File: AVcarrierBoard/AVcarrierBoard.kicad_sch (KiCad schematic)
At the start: 16 parts, among them J1 Mech_Switch, J2 Mech_Switch, J3 MainRecov, J4 DrogRecov, J5 Staging, J6 Mech_Switch, U2 WiFi Switch, U3 EggtimerQuantum, U4 EggfinderMini/FeatherGPS, U5 Blue_Raven

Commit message: final edits made, order placed
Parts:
- BT1: symbol Device:Battery -> COTS_boards:Battery
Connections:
- net GND: now also BT1.3 (-); no longer BT1.2 (-)
- new net: BT1.2 (middle), BT1.4 (middle)
- no-connect marks 0 -> 1
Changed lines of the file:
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@@
 (kicad_sch (version 20230121) (generator eeschema)
   (paper "A4")
+  (no_connect (at 31.75 52.07))
   (rectangle (start 86.995 154.94) (end 142.875 179.07)
     (stroke (width 0.2) (type dash))
@@
     )
   )
-  (symbol (lib_id "Device:Battery") (at 33.655 52.705 0) (unit 1)
-    (in_bom yes) (on_board yes) (dnp no) (fields_autoplaced)
-    (property "Reference" "BT1" (at 37.465 50.8635 0)
-      (effects (font (size 1.27 1.27)) (justify left))
-    )
-    (property "Value" "Batt_2S" (at 37.465 53.4035 0)
-      (effects (font (size 1.27 1.27)) (justify left))
-    )
-    (property "Footprint" "COTS_Boards:BAT_1048P" (at 33.655 51.181 90)
-      (effects (font (size 1.27 1.27)) hide)
-    )
-    (property "Datasheet" "~" (at 33.655 51.181 90)
-      (effects (font (size 1.27 1.27)) hide)
-    )
-    (pin "1")
-    (pin "2")
-    (instances
-      (project "AVcarrierBoard"
-        (path "/7d4c9aa4-eccf-4732-8f5d-af2c3b6d9138"
-          (reference "BT1") (unit 1)
-        )
-      )
-    )
-  )
-  (symbol (lib_id "Mechanical:MountingHole") (at 64.77 162.56 0) (unit 1)
-    (in_bom yes) (on_board yes) (dnp no) (fields_autoplaced)
-    (property "Reference" "H4" (at 67.31 161.29 0)
-      (effects (font (size 1.27 1.27)) (justify left))
-    )
-    (property "Value" "M3" (at 67.31 163.83 0)
-      (effects (font (size 1.27 1.27)) (justify left))
-    )
-    (property "Footprint" "MountingHole:MountingHole_3.2mm_M3_ISO14580" (at 64.77 162.56 0)
-      (effects (font (size 1.27 1.27)) hide)
-    )
-    (property "Datasheet" "~" (at 64.77 162.56 0)
-      (effects (font (size 1.27 1.27)) hide)
-    )
-    (instances
-      (project "AVcarrierBoard"
-        (path "/7d4c9aa4-eccf-4732-8f5d-af2c3b6d9138"
-          (reference "H4") (unit 1)
-        )
-      )
-    )
-  )
-  (symbol (lib_id "power:+7.5V") (at 33.655 47.625 0) (unit 1)
-    (in_bom yes) (on_board yes) (dnp no)
-    (property "Reference" "#PWR04" (at 33.655 51.435 0)
-      (effects (font (size 1.27 1.27)) hide)
-    )
-    (property "Value" "+7.5V" (at 33.655 42.545 0)
-      (effects (font (size 1.27 1.27)))
-    )
-    (property "Footprint" "" (at 33.655 47.625 0)
-      (effects (font (size 1.27 1.27)) hide)
-    )
-    (property "Datasheet" "" (at 33.655 47.625 0)
-      (effects (font (size 1.27 1.27)) hide)
-    )
-    (pin "1")
-    (instances
-      (project "AVcarrierBoard"
-        (path "/7d4c9aa4-eccf-4732-8f5d-af2c3b6d9138"
-          (reference "#PWR04") (unit 1)
-        )
-      )
-    )
-  )
-  (symbol (lib_id "Device:Battery_Cell") (at 33.655 111.125 0) (unit 1)
-    (in_bom yes) (on_board yes) (dnp no) (fields_autoplaced)
-    (property "Reference" "BT2" (at 37.465 108.0135 0)
-      (effects (font (size 1.27 1.27)) (justify left))
-    )
-    (property "Value" "Batt_1S" (at 37.465 110.5535 0)
-      (effects (font (size 1.27 1.27)) (justify left))
-    )
-    (property "Footprint" "COTS_Boards:1042P_KEY" (at 33.655 109.601 90)
-      (effects (font (size 1.27 1.27)) hide)
-    )
-    (property "Datasheet" "~" (at 33.655 109.601 90)
-      (effects (font (size 1.27 1.27)) hide)
-    )
-    (pin "1")
-    (pin "2")
-    (instances
-      (project "AVcarrierBoard"
-        (path "/7d4c9aa4-eccf-4732-8f5d-af2c3b6d9138"
-          (reference "BT2") (unit 1)
-        )
-      )
-    )
-  )
-  (symbol (lib_id "Connector:Screw_Terminal_01x04") (at 257.81 51.435 0) (unit 1)
-    (in_bom yes) (on_board yes) (dnp no) (fields_autoplaced)
-    (property "Reference" "J3" (at 260.35 51.435 0)
-      (effects (font (size 1.27 1.27)) (justify left))
-    )
-    (property "Value" "MainRecov" (at 260.35 53.975 0)
-      (effects (font (size 1.27 1.27)) (justify left))
-    )
-    (property "Footprint" "COTS_Boards:TE_282837-4-2" (at 257.81 51.435 0)
-      (effects (font (size 1.27 1.27)) hide)
-    )
-    (property "Datasheet" "~" (at 257.81 51.435 0)
-      (effects (font (size 1.27 1.27)) hide)
-    )
+  (symbol (lib_id "COTS_boards:Battery") (at 34.29 52.07 0) (unit 1)
+    (in_bom yes) (on_board yes) (dnp no) (fields_autoplaced)
+    (property "Reference" "BT1" (at 37.465 50.2285 0)
+      (effects (font (size 1.27 1.27)) (justify left))
+    )
+    (property "Value" "Batt_2S" (at 37.465 52.7685 0)
+      (effects (font (size 1.27 1.27)) (justify left))
+    )
+    (property "Footprint" "COTS_Boards:BAT_1048P" (at 34.29 50.546 90)
+      (effects (font (size 1.27 1.27)) hide)
+    )
+    (property "Datasheet" "~" (at 34.29 50.546 90)
+      (effects (font (size 1.27 1.27)) hide)
+    )
+    (pin "1")
     (pin "4")
     (pin "3")
     (pin "2")
+    (instances
+      (project "AVcarrierBoard"
+        (path "/7d4c9aa4-eccf-4732-8f5d-af2c3b6d9138"
+          (reference "BT1") (unit 1)
+        )
+      )
+    )
+  )
+  (symbol (lib_id "Mechanical:MountingHole") (at 64.77 162.56 0) (unit 1)
+    (in_bom yes) (on_board yes) (dnp no) (fields_autoplaced)
+    (property "Reference" "H4" (at 67.31 161.29 0)
+      (effects (font (size 1.27 1.27)) (justify left))
+    )
+    (property "Value" "M3" (at 67.31 163.83 0)
+      (effects (font (size 1.27 1.27)) (justify left))
+    )
+    (property "Footprint" "MountingHole:MountingHole_3.2mm_M3_ISO14580" (at 64.77 162.56 0)
+      (effects (font (size 1.27 1.27)) hide)
+    )
+    (property "Datasheet" "~" (at 64.77 162.56 0)
+      (effects (font (size 1.27 1.27)) hide)
+    )
+    (instances
+      (project "AVcarrierBoard"
+        (path "/7d4c9aa4-eccf-4732-8f5d-af2c3b6d9138"
+          (reference "H4") (unit 1)
+        )
+      )
+    )
+  )
+  (symbol (lib_id "power:+7.5V") (at 34.29 46.99 0) (unit 1)
+    (in_bom yes) (on_board yes) (dnp no)
+    (property "Reference" "#PWR04" (at 34.29 50.8 0)
+      (effects (font (size 1.27 1.27)) hide)
+    )
+    (property "Value" "+7.5V" (at 34.29 41.91 0)
+      (effects (font (size 1.27 1.27)))
+    )
+    (property "Footprint" "" (at 34.29 46.99 0)
+      (effects (font (size 1.27 1.27)) hide)
+    )
+    (property "Datasheet" "" (at 34.29 46.99 0)
+      (effects (font (size 1.27 1.27)) hide)
+    )
+    (pin "1")
+    (instances
+      (project "AVcarrierBoard"
+        (path "/7d4c9aa4-eccf-4732-8f5d-af2c3b6d9138"
+          (reference "#PWR04") (unit 1)
+        )
+      )
+    )
+  )
+  (symbol (lib_id "Device:Battery_Cell") (at 33.655 111.125 0) (unit 1)
+    (in_bom yes) (on_board yes) (dnp no) (fields_autoplaced)
+    (property "Reference" "BT2" (at 37.465 108.0135 0)
+      (effects (font (size 1.27 1.27)) (justify left))
+    )
+    (property "Value" "Batt_1S" (at 37.465 110.5535 0)
+      (effects (font (size 1.27 1.27)) (justify left))
+    )
+    (property "Footprint" "COTS_Boards:1042P_KEY" (at 33.655 109.601 90)
+      (effects (font (size 1.27 1.27)) hide)
+    )
+    (property "Datasheet" "~" (at 33.655 109.601 90)
+      (effects (font (size 1.27 1.27)) hide)
+    )
+    (pin "1")
+    (pin "2")
+    (instances
+      (project "AVcarrierBoard"
+        (path "/7d4c9aa4-eccf-4732-8f5d-af2c3b6d9138"
+          (reference "BT2") (unit 1)
+        )
+      )
+    )
+  )
+  (symbol (lib_id "Connector:Screw_Terminal_01x04") (at 257.81 51.435 0) (unit 1)
+    (in_bom yes) (on_board yes) (dnp no) (fields_autoplaced)
+    (property "Reference" "J3" (at 260.35 51.435 0)
+      (effects (font (size 1.27 1.27)) (justify left))
+    )
+    (property "Value" "MainRecov" (at 260.35 53.975 0)
+      (effects (font (size 1.27 1.27)) (justify left))
+    )
+    (property "Footprint" "COTS_Boards:TE_282837-4-2" (at 257.81 51.435 0)
+      (effects (font (size 1.27 1.27)) hide)
+    )
+    (property "Datasheet" "~" (at 257.81 51.435 0)
+      (effects (font (size 1.27 1.27)) hide)
+    )
+    (pin "4")
+    (pin "3")
+    (pin "2")
     (pin "1")
     (instances
@@
     )
   )
-  (symbol (lib_id "power:GND") (at 33.655 57.785 0) (unit 1)
-    (in_bom yes) (on_board yes) (dnp no) (fields_autoplaced)
-    (property "Reference" "#PWR01" (at 33.655 64.135 0)
-      (effects (font (size 1.27 1.27)) hide)
-    )
-    (property "Value" "GND" (at 33.655 62.865 0)
-      (effects (font (size 1.27 1.27)))
-    )
-    (property "Footprint" "" (at 33.655 57.785 0)
-      (effects (font (size 1.27 1.27)) hide)
-    )
-    (property "Datasheet" "" (at 33.655 57.785 0)
-      (effects (font (size 1.27 1.27)) hide)
-    )
+  (symbol (lib_id "power:GND") (at 34.29 57.15 0) (unit 1)
+    (in_bom yes) (on_board yes) (dnp no) (fields_autoplaced)
+    (property "Reference" "#PWR01" (at 34.29 63.5 0)
+      (effects (font (size 1.27 1.27)) hide)
+    )
+    (property "Value" "GND" (at 34.29 62.23 0)
+      (effects (font (size 1.27 1.27)))
+    )
+    (property "Footprint" "" (at 34.29 57.15 0)
+      (effects (font (size 1.27 1.27)) hide)
+    )
+    (property "Datasheet" "" (at 34.29 57.15 0)
+      (effects (font (size 1.27 1.27)) hide)
+    )

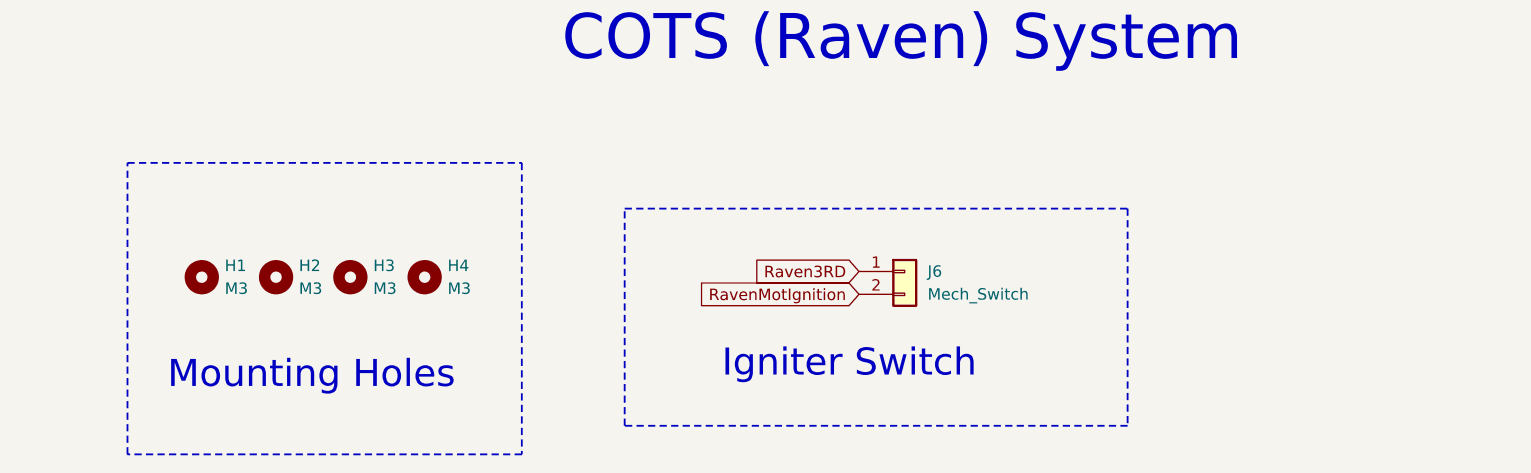
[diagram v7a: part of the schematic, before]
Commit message: Added mounting holes for battery holders
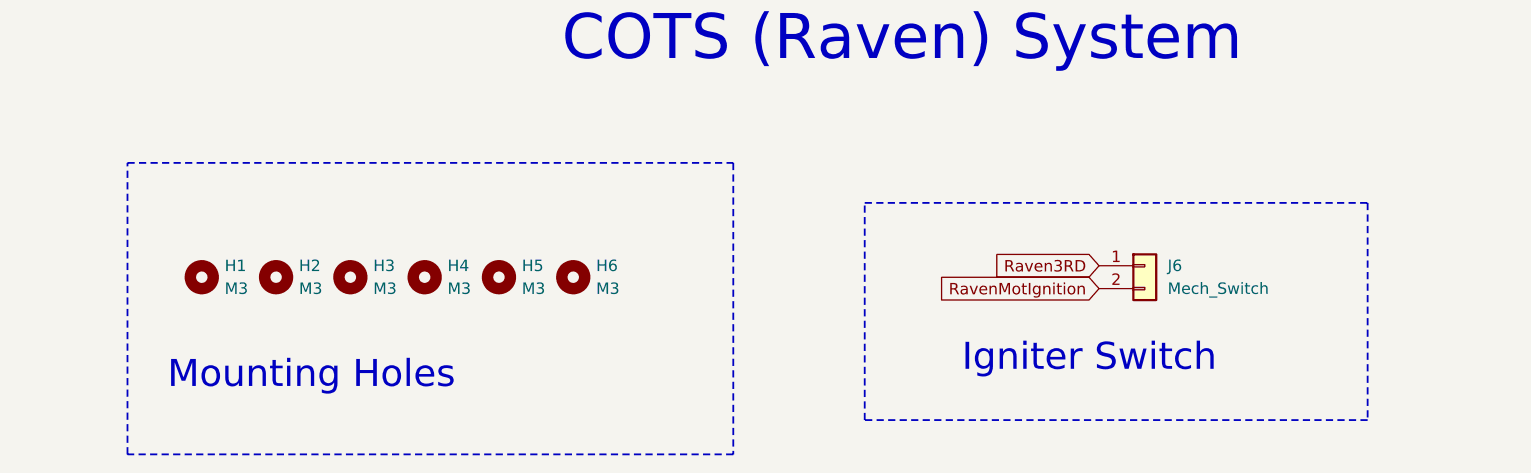
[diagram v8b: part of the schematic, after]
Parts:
- added H5, H6: M3, MountingHole:MountingHole_3.2mm_M3_ISO14580, symbol Mechanical:MountingHole
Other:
- moved on the sheet: J6
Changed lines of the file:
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@@
   (paper "A4")
   (no_connect (at 31.75 52.07))
-  (rectangle (start 86.995 154.94) (end 142.875 179.07)
+  (rectangle (start 113.665 154.305) (end 169.545 178.435)
     (stroke (width 0.2) (type dash))
     (fill (type none))
@@
     (fill (type none))
   )
-  (rectangle (start 31.75 149.86) (end 75.565 182.245)
+  (rectangle (start 31.75 149.86) (end 99.06 182.245)
     (stroke (width 0.2) (type dash))
     (fill (type none))
@@
     (effects (font (face "KiCad Font") (size 3 3)) (justify left bottom))
   )
-  (text "Igniter Switch" (at 97.79 173.99 0)
+  (text "Igniter Switch" (at 124.46 173.355 0)
     (effects (font (face "KiCad Font") (size 3 3)) (justify left bottom))
   )
@@
     )
   )
-  (global_label "RavenMotIgnition" (shape input) (at 113.03 164.465 180) (fields_autoplaced)
-    (effects (font (size 1.27 1.27)) (justify right))
-    (property "Intersheetrefs" "${INTERSHEET_REFS}" (at 93.9584 164.465 0)
+  (global_label "RavenMotIgnition" (shape input) (at 139.7 163.83 180) (fields_autoplaced)
+    (effects (font (size 1.27 1.27)) (justify right))
+    (property "Intersheetrefs" "${INTERSHEET_REFS}" (at 120.6284 163.83 0)
       (effects (font (size 1.27 1.27)) (justify right) hide)
     )
@@
     )
   )
-  (global_label "Raven3RD" (shape input) (at 113.03 161.925 180) (fields_autoplaced)
-    (effects (font (size 1.27 1.27)) (justify right))
-    (property "Intersheetrefs" "${INTERSHEET_REFS}" (at 100.6711 161.925 0)
+  (global_label "Raven3RD" (shape input) (at 139.7 161.29 180) (fields_autoplaced)
+    (effects (font (size 1.27 1.27)) (justify right))
+    (property "Intersheetrefs" "${INTERSHEET_REFS}" (at 127.3411 161.29 0)
       (effects (font (size 1.27 1.27)) (justify right) hide)
     )
@@
     )
   )
-  (symbol (lib_id "Connector_Generic:Conn_01x02") (at 118.11 161.925 0) (unit 1)
-    (in_bom yes) (on_board yes) (dnp no) (fields_autoplaced)
-    (property "Reference" "J6" (at 120.65 161.925 0)
-      (effects (font (size 1.27 1.27)) (justify left))
-    )
-    (property "Value" "Mech_Switch" (at 120.65 164.465 0)
-      (effects (font (size 1.27 1.27)) (justify left))
-    )
-    (property "Footprint" "Connector_PinHeader_2.54mm:PinHeader_1x02_P2.54mm_Vertical" (at 118.11 161.925 0)
-      (effects (font (size 1.27 1.27)) hide)
-    )
-    (property "Datasheet" "~" (at 118.11 161.925 0)
+  (symbol (lib_id "Connector_Generic:Conn_01x02") (at 144.78 161.29 0) (unit 1)
+    (in_bom yes) (on_board yes) (dnp no) (fields_autoplaced)
+    (property "Reference" "J6" (at 147.32 161.29 0)
+      (effects (font (size 1.27 1.27)) (justify left))
+    )
+    (property "Value" "Mech_Switch" (at 147.32 163.83 0)
+      (effects (font (size 1.27 1.27)) (justify left))
+    )
+    (property "Footprint" "Connector_PinHeader_2.54mm:PinHeader_1x02_P2.54mm_Vertical" (at 144.78 161.29 0)
+      (effects (font (size 1.27 1.27)) hide)
+    )
+    (property "Datasheet" "~" (at 144.78 161.29 0)
       (effects (font (size 1.27 1.27)) hide)
     )
@@
     )
   )
+  (symbol (lib_id "Mechanical:MountingHole") (at 73.025 162.56 0) (unit 1)
+    (in_bom yes) (on_board yes) (dnp no) (fields_autoplaced)
+    (property "Reference" "H5" (at 75.565 161.29 0)
+      (effects (font (size 1.27 1.27)) (justify left))
+    )
+    (property "Value" "M3" (at 75.565 163.83 0)
+      (effects (font (size 1.27 1.27)) (justify left))
+    )
+    (property "Footprint" "MountingHole:MountingHole_3.2mm_M3_ISO14580" (at 73.025 162.56 0)
+      (effects (font (size 1.27 1.27)) hide)
+    )
+    (property "Datasheet" "~" (at 73.025 162.56 0)
+      (effects (font (size 1.27 1.27)) hide)
+    )
+    (instances
+      (project "AVcarrierBoard"
+        (path "/7d4c9aa4-eccf-4732-8f5d-af2c3b6d9138"
+          (reference "H5") (unit 1)
+        )
+      )
+    )
+  )
   (symbol (lib_id "COTS_boards:EggfinderMini") (at 182.88 62.865 0) (mirror y) (unit 1)
     (in_bom yes) (on_board yes) (dnp no)
@@
         )
       )
+    )
+  )
+  (symbol (lib_id "Mechanical:MountingHole") (at 81.28 162.56 0) (unit 1)
+    (in_bom yes) (on_board yes) (dnp no) (fields_autoplaced)
+    (property "Reference" "H6" (at 83.82 161.29 0)
+      (effects (font (size 1.27 1.27)) (justify left))
+    )
+    (property "Value" "M3" (at 83.82 163.83 0)
+      (effects (font (size 1.27 1.27)) (justify left))
+    )
+    (property "Footprint" "MountingHole:MountingHole_3.2mm_M3_ISO14580" (at 81.28 162.56 0)
+      (effects (font (size 1.27 1.27)) hide)
+    )
+    (property "Datasheet" "~" (at 81.28 162.56 0)
+      (effects (font (size 1.27 1.27)) hide)
+    )
+    (instances
+      (project "AVcarrierBoard"
+        (path "/7d4c9aa4-eccf-4732-8f5d-af2c3b6d9138"
+          (reference "H6") (unit 1)
+        )
+      )
